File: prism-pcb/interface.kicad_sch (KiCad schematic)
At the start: 13 parts, among them J301 Conn_01x04_P3.5mm_TBH_Horizon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, M301 Fan_5VDC_25x25x8mm, U301 TPSM365R6V5RDNR

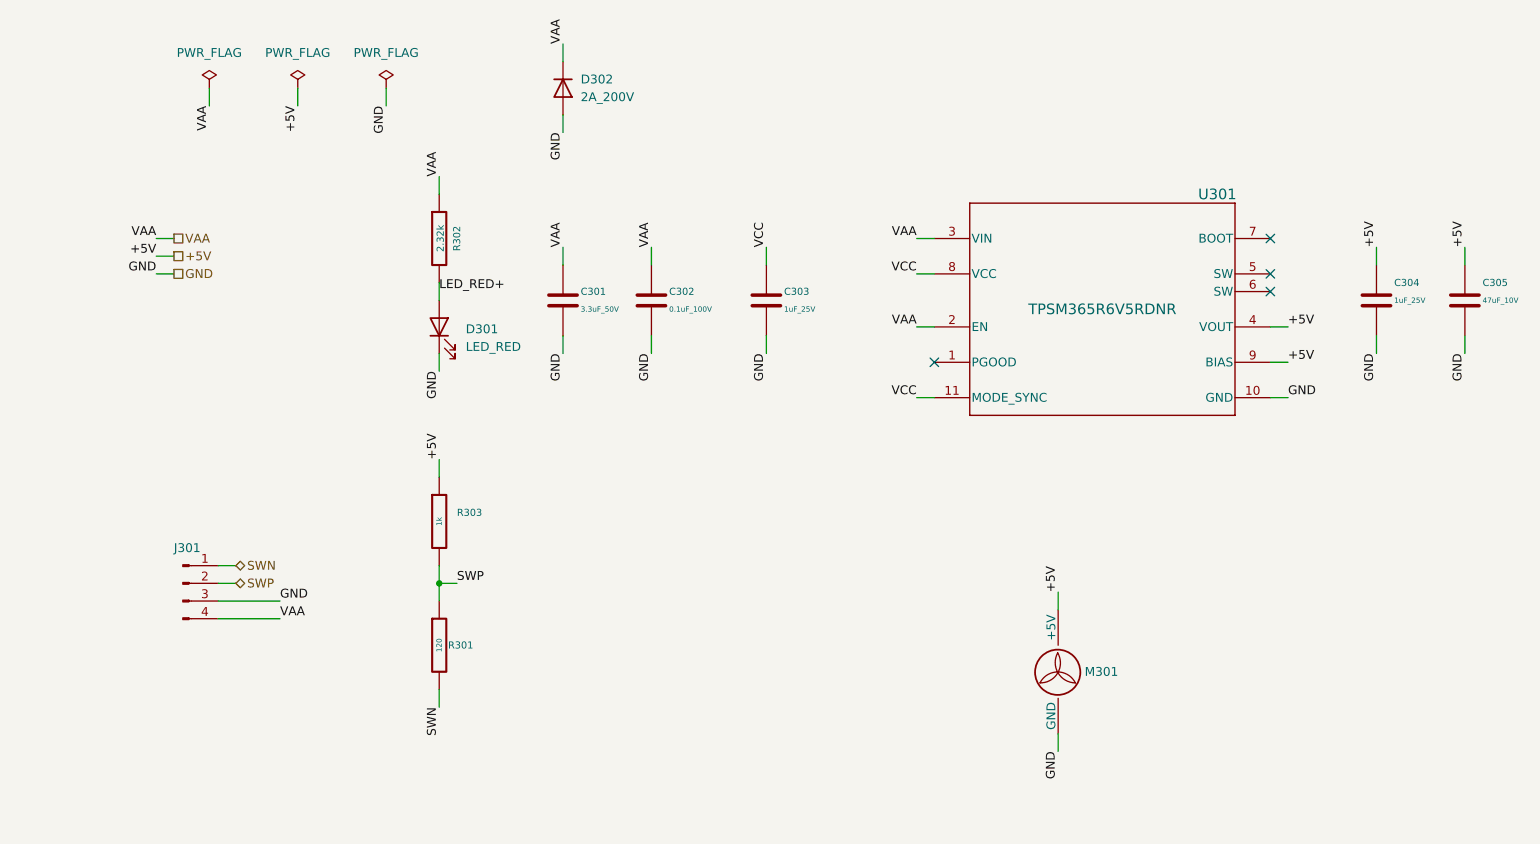
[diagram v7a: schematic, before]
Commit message: Switch to USB connector
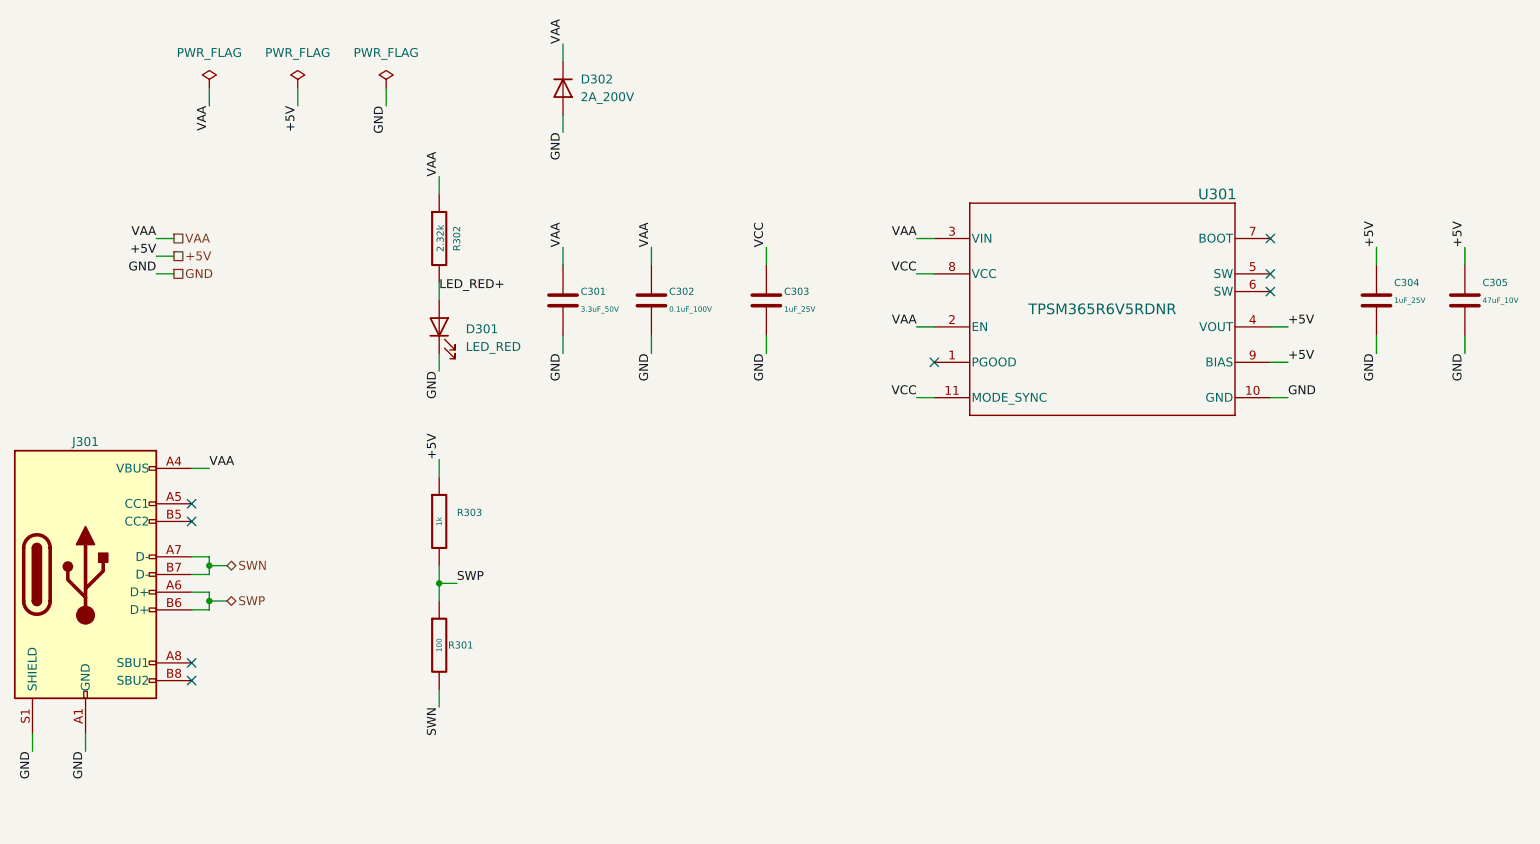
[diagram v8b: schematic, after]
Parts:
- removed J301: Conn_01x04_P3.5mm_TBH_Horizontal_Screw, Janelia:PhoenixContact_MC_1,5_4-G-3.5_1x04_P3.50mm_Horizontal_Screw, symbol Janelia:Conn_01x04_P3.5mm_TBH_Horizontal_Screw
- removed M301: Fan_5VDC_25x25x8mm, Janelia:FAN_5VDC_25x25x8mm, symbol Janelia:Fan_5VDC_25x25x8mm
- removed R301: 120, Janelia:R_0402_1005Metric, symbol Janelia:R_120_0402
- added J301: Connector_USB_C_Receptacle_USB2.0_16P_GT-USB-7047C, Janelia:USB_C_Receptacle_GT-USB-7047C_16P_TopMnt_Horizontal, symbol Janelia:Connector_USB_C_Receptacle_USB2.0_16P_GT-USB-7047C
- added R301: 100, Janelia:R_0402_1005Metric, symbol Janelia:R_100_0402
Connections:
- net GND: now also J301.A1 (GND), J301.A12 (GND), J301.B1 (GND), J301.B12 (GND), J301.S1 (SHIELD)
- net SWN: now also J301.A7 (D-), J301.B7 (D-), R301.2
- net SWP: now also J301.A6 (D+), J301.B6 (D+), R301.1
- net VAA: now also J301.A4 (VBUS), J301.A9 (VBUS), J301.B4 (VBUS), J301.B9 (VBUS)
- no-connect marks 4 -> 8
